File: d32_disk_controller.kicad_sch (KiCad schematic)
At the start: 25 parts, among them J1 Clock_Test, J2 IDC_Floppy, J3 EDGE, U1 27C64, U2 WD2797, U3 74LS174, U4 74LS139, U5 74LS00, U6 7416, U7 7417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

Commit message: verify component availability
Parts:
- U3: value 74LS174 -> 74HCT174; footprint Package_SO:SOIC-16W_7.5x10.3mm_P1.27mm -> Package_SO:SOIC-16W_5.3x10.2mm_P1.27mm; DigiKey (none) -> 296-9260-5-ND
- U4: value 74LS139 -> 74HCT139; footprint Package_SO:SOIC-16W_7.5x10.3mm_P1.27mm -> Package_SO:SOIC-16W_5.3x10.2mm_P1.27mm; DigiKey (none) -> 296-SN74HCT139DBRCT-ND
- U5: value 74LS00 -> 74HCT00; footprint Package_SO:SOIC-14W_7.5x9mm_P1.27mm -> Package_SO:SOIC-14_3.9x8.7mm_P1.27mm; DigiKey (none) -> 296-14860-1-ND
- U6: value 7416 -> 74HCT04; footprint Package_SO:SOIC-14W_7.5x9mm_P1.27mm -> Package_SO:SOIC-14_3.9x8.7mm_P1.27mm; DigiKey (none) -> 296-1205-1-ND
- U7: value 7417 -> 74LS07; footprint Package_SO:SOIC-14W_7.5x9mm_P1.27mm -> Package_SO:SOIC-14_3.9x8.7mm_P1.27mm; DigiKey (none) -> 296-14877-1-ND
- U8: value 74LS74 -> 74HCT74; footprint Package_SO:SOIC-14W_7.5x9mm_P1.27mm -> Package_SO:SOIC-14_3.9x8.7mm_P1.27mm; DigiKey (none) -> 296-1211-1-ND
- U9: value 74LS04 -> 74HCT04; footprint Package_SO:SOIC-14W_7.5x9mm_P1.27mm -> Package_SO:SOIC-14_3.9x8.7mm_P1.27mm; DigiKey (none) -> 296-1205-1-ND
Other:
- title: (none) -> Dragon 32/64 Disk Controller

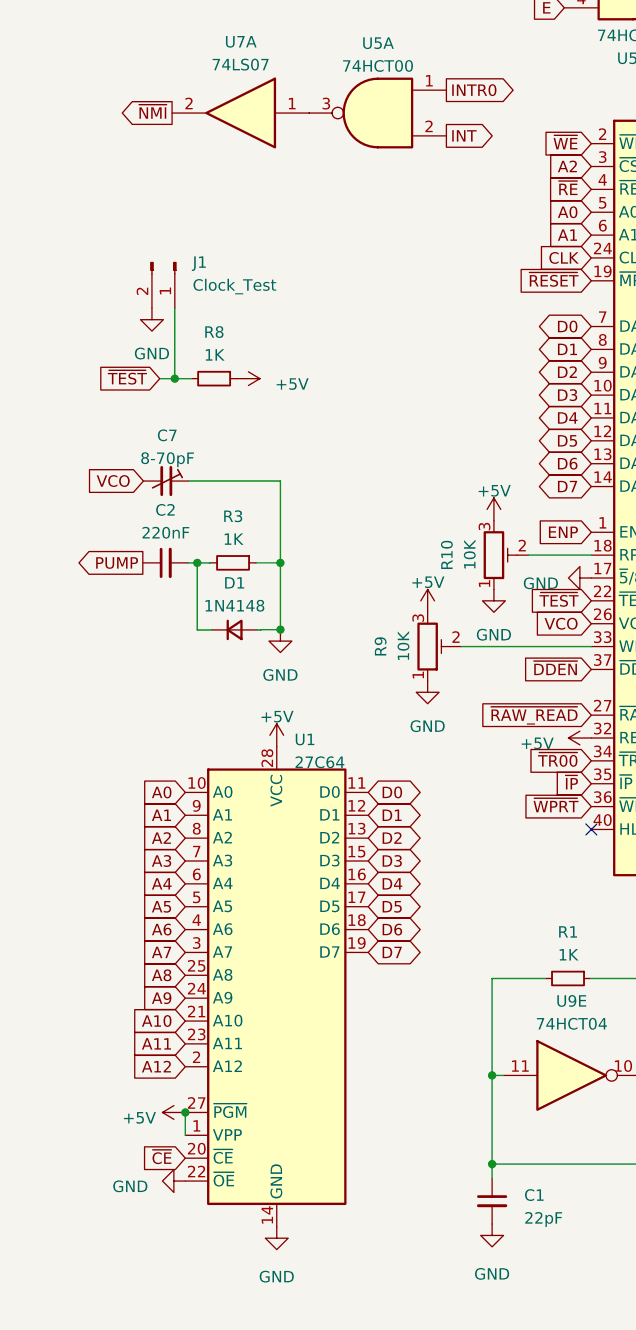
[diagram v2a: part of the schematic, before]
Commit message: revise board for better component selection
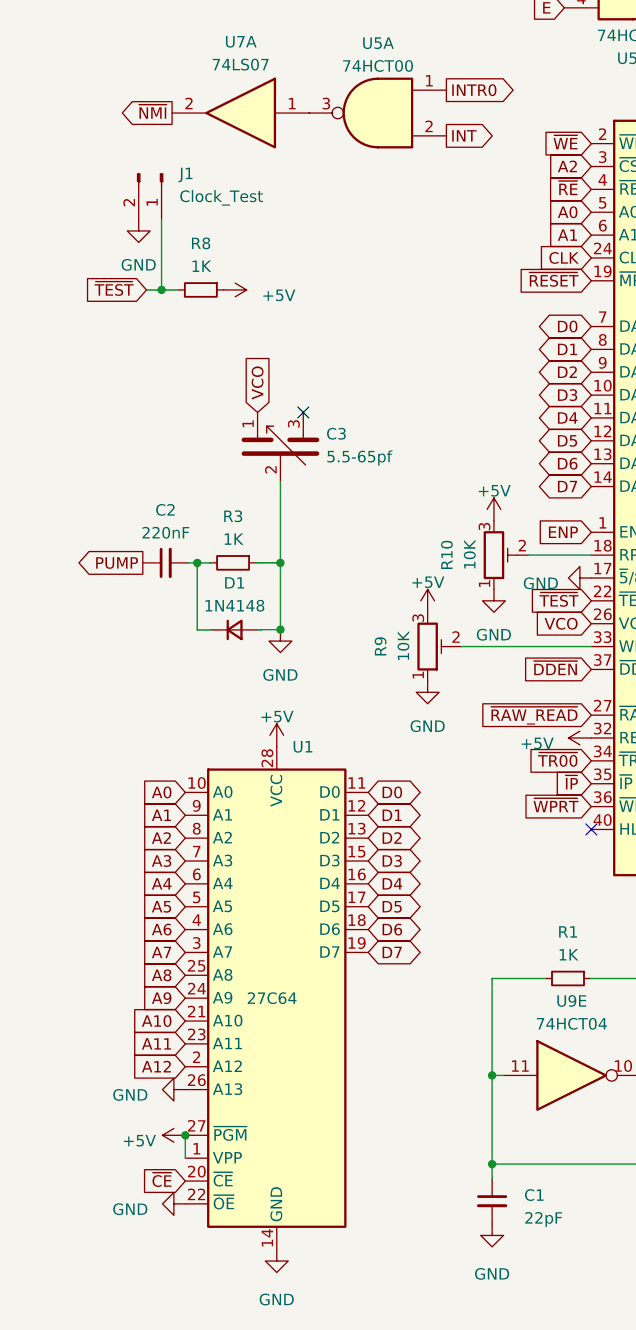
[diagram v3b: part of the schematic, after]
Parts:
- removed C7: 8-70pF, Potentiometer_THT:Potentiometer_Vishay_T73YP_Vertical, symbol Device:C_Trim_Small
- added C3: 5.5-65pf, d32_cart:Trimmer-10mm, symbol Device:C_Trim_Differential
- R10, R9: footprint Potentiometer_SMD:Potentiometer_Bourns_3224X_Vertical -> Potentiometer_THT:Potentiometer_Bourns_3296Y_Vertical
- U1: symbol Memory_EPROM:27C64 -> Memory_EPROM:27C128
- U3, U4: footprint Package_SO:SOIC-16W_5.3x10.2mm_P1.27mm -> Package_SO:SOIC-16_3.9x9.9mm_P1.27mm
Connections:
- net GND: now also U1.26 (A13), C3.2
- net VCO: now also C3.1
- no-connect marks 21 -> 22
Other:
- moved on the sheet: J1, R8

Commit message: prepare for cpld
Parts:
- removed C1: 22pF, Capacitor_SMD:C_0805_2012Metric_Pad1.18x1.45mm_HandSolder, symbol Device:C_Small
- removed C8: 10nF, Capacitor_SMD:C_0805_2012Metric_Pad1.18x1.45mm_HandSolder, symbol Device:C_Small
- removed R1, R2: 1K, Resistor_SMD:R_0805_2012Metric_Pad1.20x1.40mm_HandSolder, symbol Device:R_Small
- removed Y1: 4MHz, Crystal:Crystal_HC18-U_Vertical, symbol Device:Crystal
- added U10: ATF1504AS-xAx44, Package_QFP:TQFP-44_10x10mm_P0.8mm, symbol CPLD_Microchip:ATF1504AS-xAx44
- added Y1: 4MHz, Oscillator:Oscillator_SMD_Abracon_ASV-4Pin_7.0x5.1mm, symbol Oscillator:ASV-xxxMHz
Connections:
- net +5V: now also U10.17 (VCC), U10.29 (VCC), U10.41 (VCC), U10.9 (VCC), Y1.4 (Vdd)
- net GND: now also U10.16 (GND), U10.24 (GND), U10.36 (GND), U10.4 (GND), Y1.2 (GND); no longer U1.26 (A13)
- net raw_clock: now also U10.37 (I/GCLK1), Y1.3 (OUT); no longer U9.8
- net ~{IP}: now also RN1.2 (R1); no longer RN1.3 (R2)
- net ~{TR00}: now also RN1.3 (R2); no longer RN1.4 (R3)
- net ~{WPRT}: now also RN1.4 (R3); no longer RN1.2 (R1)
- net A13: now reaches J3.37 (Pin_37)
- net A13: now also U1.26 (A13)
- new net TCK: U10.26 (I/O/TCK)
- new net TDI: U10.1 (I/O/TDI)
- new net TDO: U10.32 (I/O/TDO)
- new net TMS: U10.7 (I/O/TMS)
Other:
- moved on the sheet: J3, RN1, U1, U4C, U5E, U6A, U6B, U6C, U6D, U6E, U6G, U7G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

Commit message: convert to small CPLD
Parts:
- removed U3: 74HCT174, Package_SO:SOIC-16_3.9x9.9mm_P1.27mm, symbol 74xx:74LS174
- removed U4: 74HCT139, Package_SO:SOIC-16_3.9x9.9mm_P1.27mm, symbol 74xx:74LS139
- removed U5: 74HCT00, Package_SO:SOIC-14_3.9x8.7mm_P1.27mm, symbol 74xx:74LS00
- removed unit 6 of U6
- removed U7: 74LS07, Package_SO:SOIC-14_3.9x8.7mm_P1.27mm, symbol Dos_Controller:7417
- removed U8: 74HCT74, Package_SO:SOIC-14_3.9x8.7mm_P1.27mm, symbol 74xx:74LS74
- removed U9: 74HCT04, Package_SO:SOIC-14_3.9x8.7mm_P1.27mm, symbol 74xx:74LS04
- added C4, C5, C6, C7: 100nF, Capacitor_SMD:C_0402_1005Metric, symbol Device:C_Small
- added J4: JTAG, Connector_PinHeader_2.54mm:PinHeader_2x05_P2.54mm_Vertical, symbol Connector_Generic:Conn_02x05_Odd_Even
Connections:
- net +5V: now also C4.2, C5.2, C6.2, C7.2, J4.4 (Pin_4)
- net A3: now also U10.22 (I/O)
- net CLK: now also U10.28 (I/O)
- net D0: now also U10.3 (I/O)
- net D1: now also U10.12 (I/O)
- net D2: now also U10.11 (I/O)
- net D3: now also U10.8 (I/O)
- net D4: now also U10.6 (I/O)
- net D5: now also U10.5 (I/O/PD1)
- net DS0: now also U10.33 (I/O)
- net DS1: now also U10.34 (I/O)
- net DS2: now also U10.35 (I/O/GCLK3)
- net DS3: now also U10.31 (I/O)
- net E: now also U10.43 (I/O)
- net ENP: now also U10.18 (I/O)
- net GND: now also C4.1, C5.1, C6.1, C7.1, J4.10 (Pin_10), J4.2 (Pin_2)
- net INTR0: now also U10.27 (I/O)
- net MOTOR: now also U10.20 (I/O)
- net P2: now also U10.21 (I/O)
- net Q: now also U10.2 (I/O)
- net R/~{W}: now also U10.25 (I/O)
- net TCK: now also J4.1 (Pin_1)
- net TDI: now also J4.9 (Pin_9)
- net TDO: now also J4.3 (Pin_3)
- net TMS: now also J4.5 (Pin_5)
- net ~{DDEN}: now also U10.15 (I/O)
- net ~{NMI}: now also U10.40 (I/OE2/GCLK2)
- net ~{RESET}: now also U10.44 (I/O), J4.6 (Pin_6)
- net ~{RE}: now also U10.23 (I/O)
- net ~{WE}: now also U10.19 (I/O/PD2)
- no-connect marks 22 -> 24
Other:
- moved on the sheet: J2, J3, RN1, U10, U6A, U6B, U6C, U6D, U6E, U6G

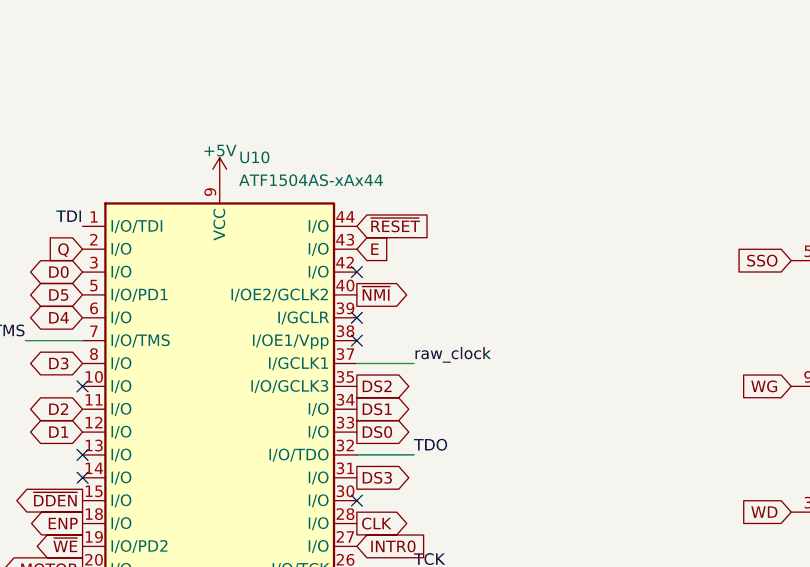
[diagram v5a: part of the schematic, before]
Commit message: add CPLD bin files
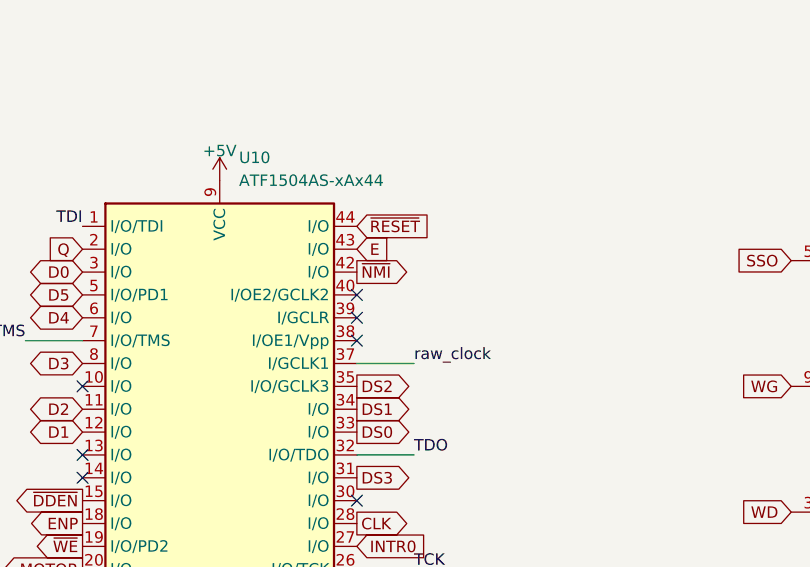
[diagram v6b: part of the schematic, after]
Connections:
- net ~{NMI}: now also U10.42 (I/O); no longer U10.40 (I/OE2/GCLK2)
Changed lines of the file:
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@@
-	)
-	(no_connect
-		(at 163.83 64.77)
 	)
 	(no_connect
@@
 	(no_connect
 		(at 39.3192 98.6993)
+	)
+	(no_connect
+		(at 163.83 67.31)
 	)
 	(no_connect
@@
 		)
 	)
-	(global_label "~{NMI}"
-		(shape output)
-		(at 163.83 67.31 0)
-		(fields_autoplaced yes)
-		(effects
-			(font
-				(size 1.27 1.27)
-			)
-			(justify left)
-		)
-		(property "Intersheetrefs" "${INTERSHEET_REFS}"
-			(at 170.1225 67.31 0)
-			(effects
-				(font
-					(size 1.27 1.27)
-				)
-				(justify left)
-				(hide yes)
-			)
-		)
-	)
 	(global_label "~{TR00}"
 		(shape input)
@@
 			(effects
 				(font
+					(size 1.27 1.27)
+				)
+				(justify left)
+				(hide yes)
+			)
+		)
+	)
+	(global_label "~{NMI}"
+		(shape output)
+		(at 163.83 64.77 0)
+		(fields_autoplaced yes)
+		(effects
+			(font
+				(size 1.27 1.27)
+			)
+			(justify left)
+		)
+		(property "Intersheetrefs" "${INTERSHEET_REFS}"
+			(at 170.1225 64.77 0)
+			(effects
+				(font

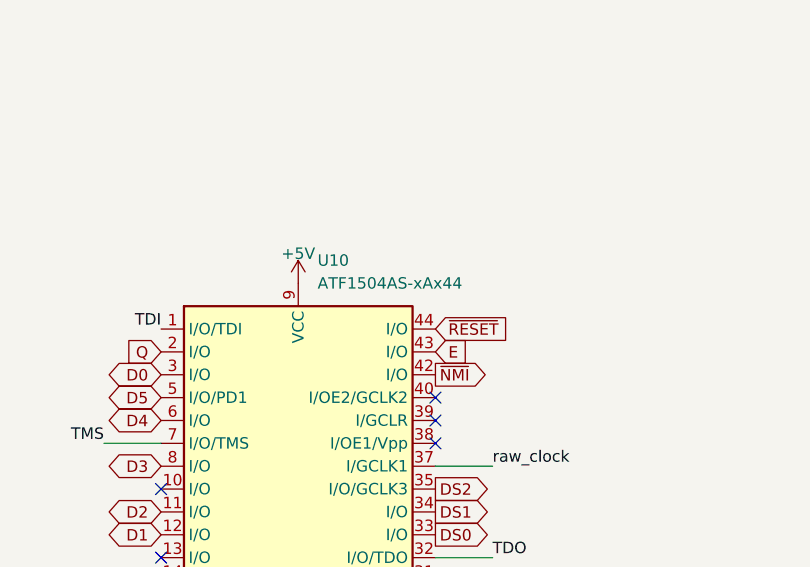
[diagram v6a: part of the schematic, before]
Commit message: change CPLD to smallest size
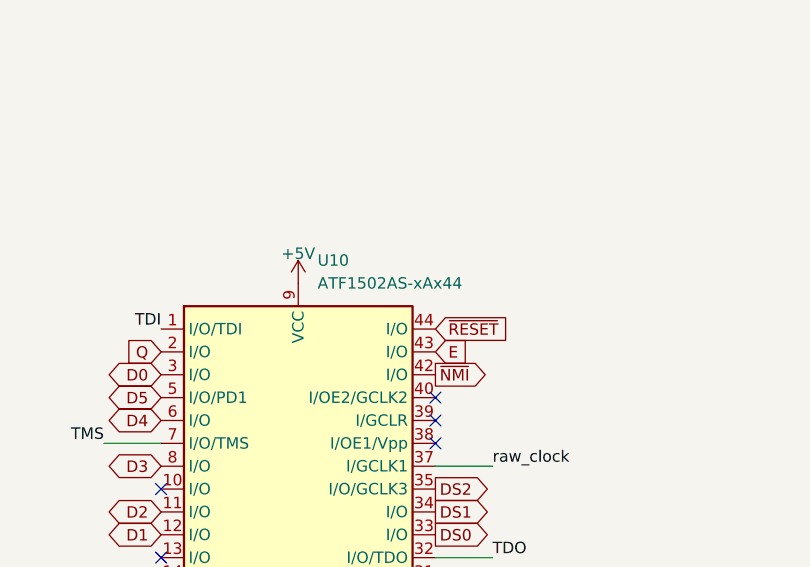
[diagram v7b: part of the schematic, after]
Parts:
- U10: value ATF1504AS-xAx44 -> ATF1502AS-xAx44
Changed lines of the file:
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@@
 			)
 		)
-		(property "Value" "ATF1504AS-xAx44"
+		(property "Value" "ATF1502AS-xAx44"
 			(at 150.7333 54.61 0)
 			(effects
@@
 			)
 		)
-		(property "Description" "Microchip CPLD, 64 Macrocell, 5 V, TQFP-44"
+		(property "Description" "Microchip CPLD, 32 Macrocell, 5 V, TQFP-44"
 			(at 148.59 80.01 0)
 			(effects
